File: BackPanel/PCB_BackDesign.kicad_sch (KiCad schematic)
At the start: 25 parts, among them J1 Conn_01x08_Pin, J2 Conn_01x09_Pin, J3 Conn_01x02_Pin, J4 Conn_01x02_Pin, SW1 KS11R23CQD, SW2 KS11R23CQD, SW3 KS11R23CQD

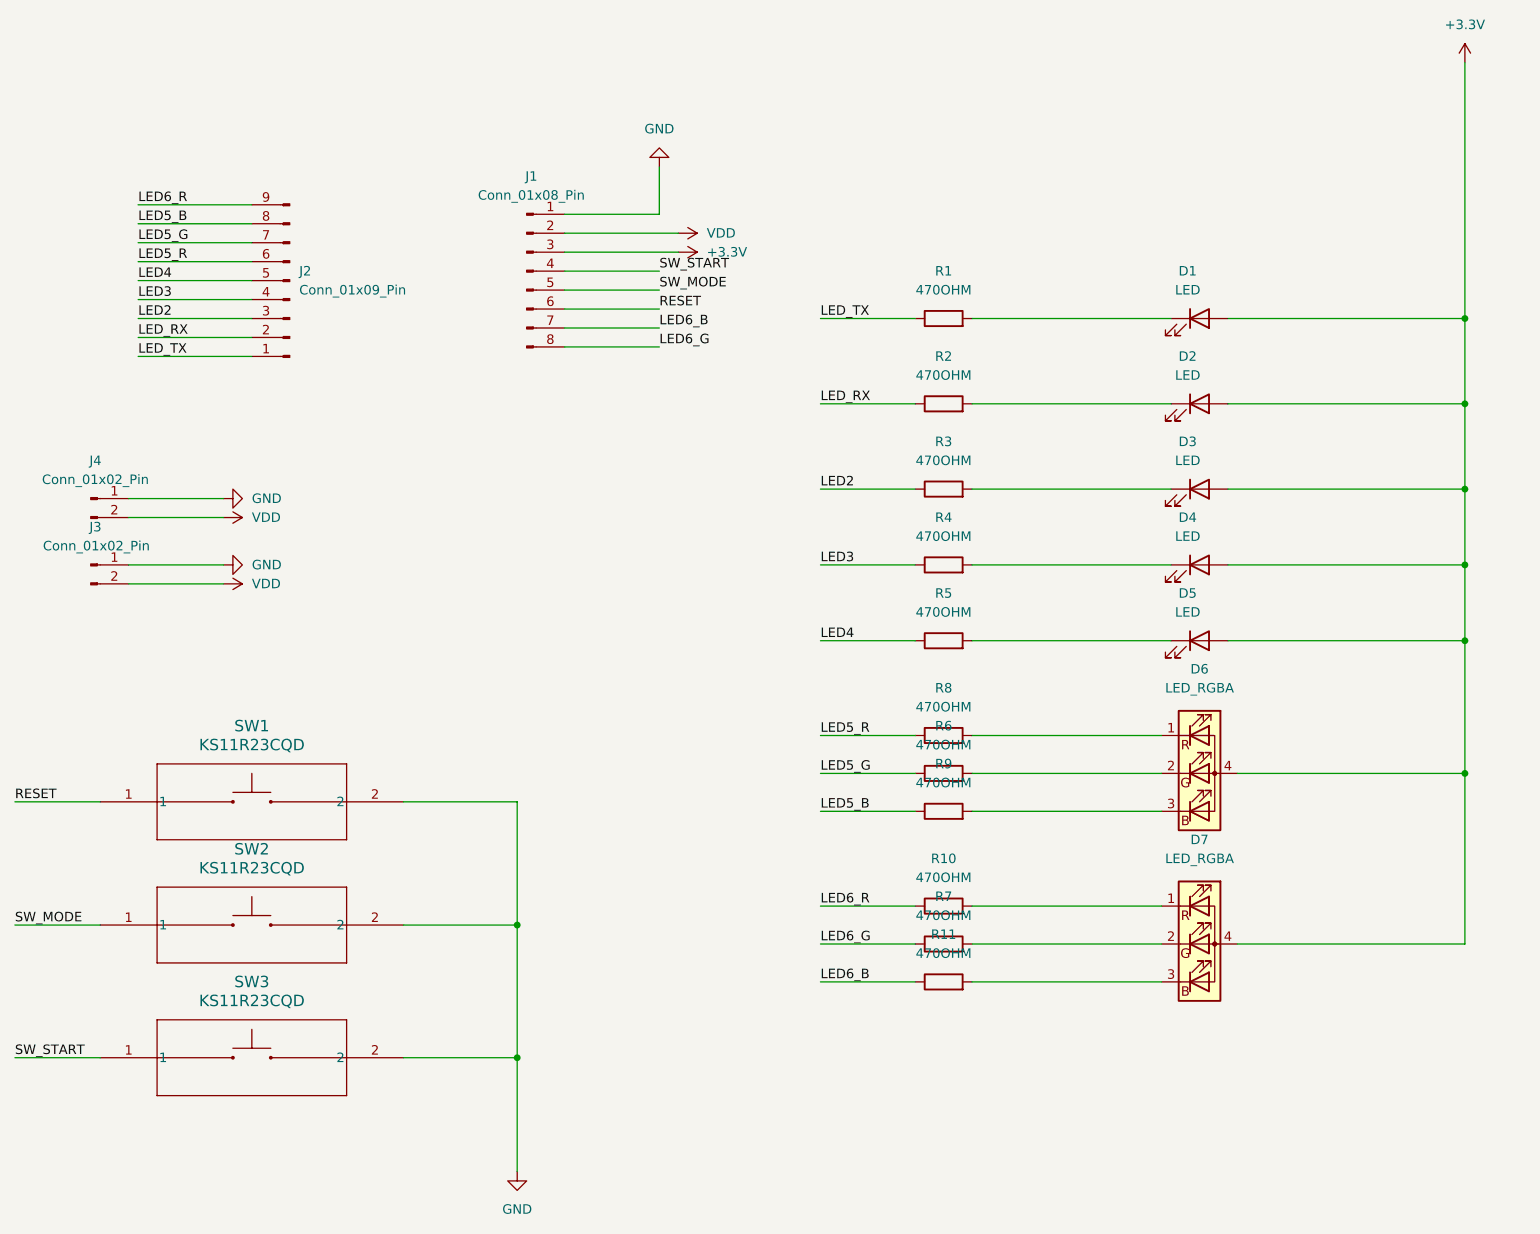
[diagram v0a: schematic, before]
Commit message: Tidied up some designators; moved two traces on the top layer to pass
DRC.
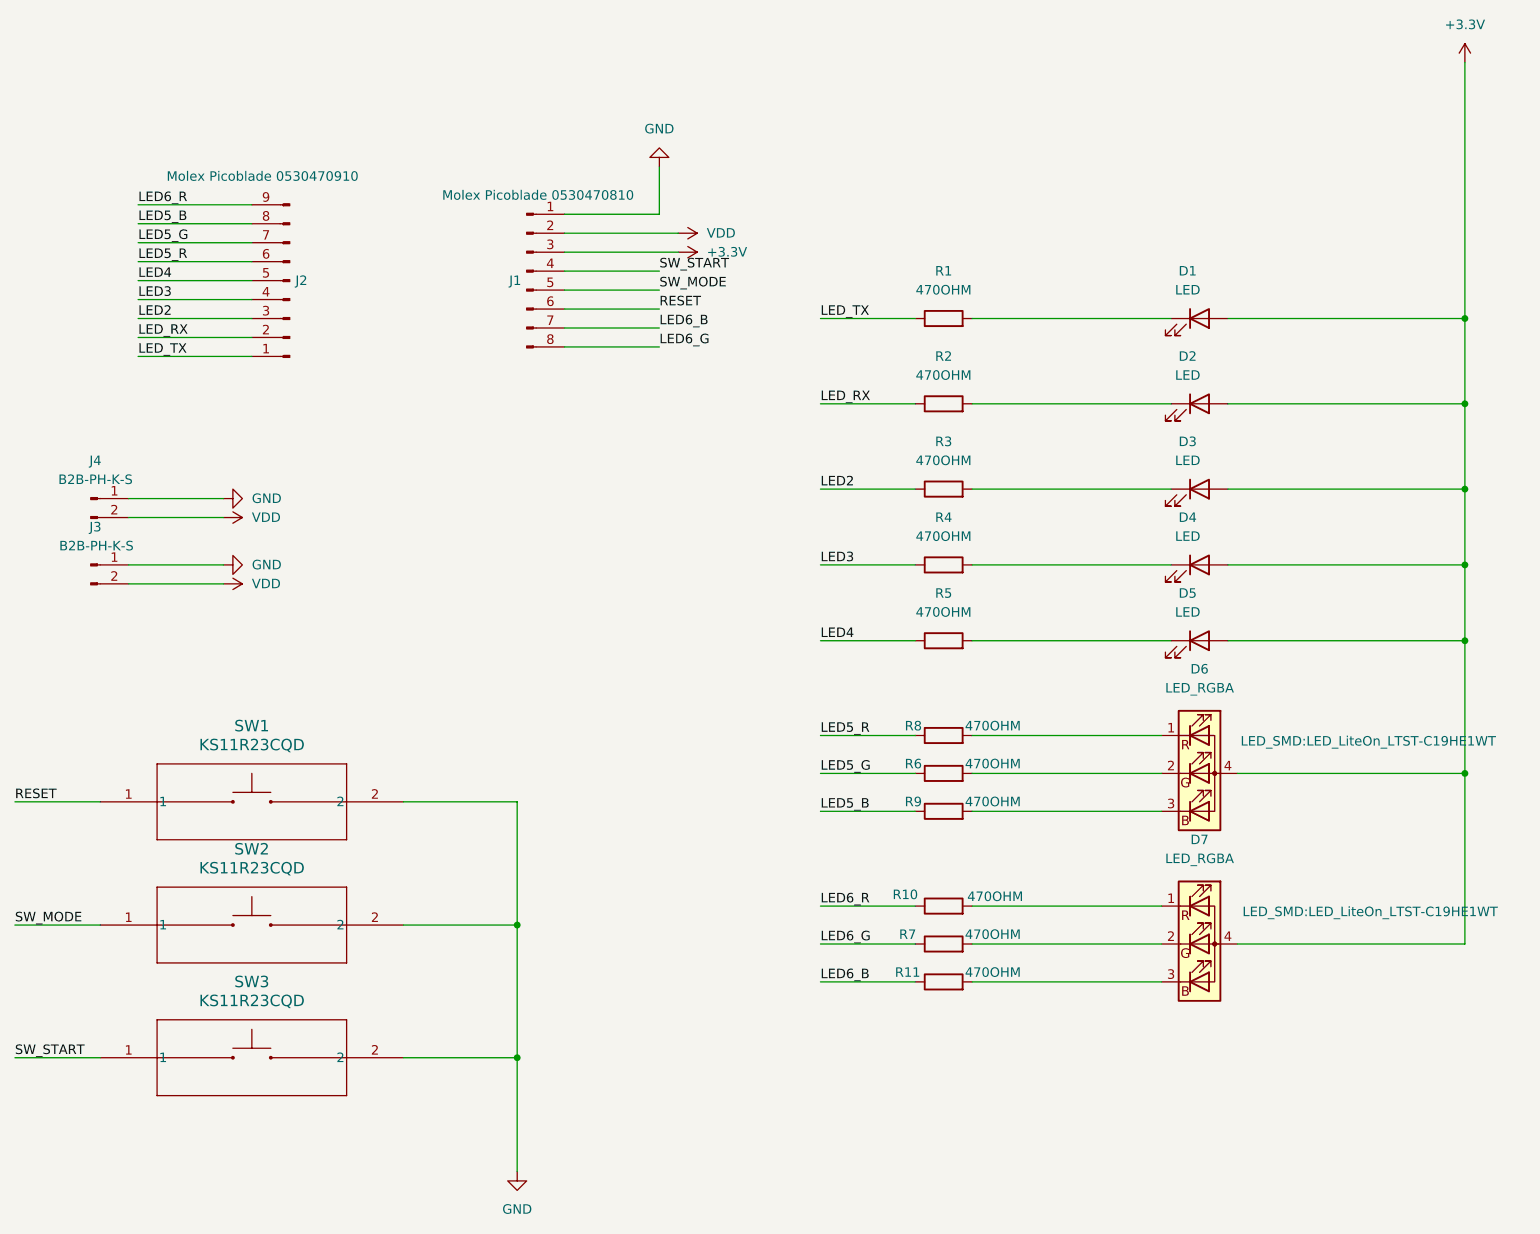
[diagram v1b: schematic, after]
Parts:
- J1: value Conn_01x08_Pin -> Molex Picoblade 0530470810
- J2: value Conn_01x09_Pin -> Molex Picoblade 0530470910
- J3, J4: value Conn_01x02_Pin -> B2B-PH-K-S
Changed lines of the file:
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@@
 		(on_board yes)
 		(dnp no)
-		(fields_autoplaced yes)
 		(property "Reference" "R10"
-			(at 184.15 132.08 90)
-			(effects
-				(font
-					(size 1.27 1.27)
-				)
+			(at 177.292 136.906 90)
+			(effects
+				(font
+					(size 1.27 1.27)
+				)
+				(justify right)
 			)
 		)
 		(property "Value" "470OHM"
-			(at 184.15 134.62 90)
-			(effects
-				(font
-					(size 1.27 1.27)
-				)
+			(at 194.818 137.16 90)
+			(effects
+				(font
+					(size 1.27 1.27)
+				)
+				(justify left)
 			)
 		)
@@
 		(on_board yes)
 		(dnp no)
-		(fields_autoplaced yes)
 		(property "Reference" "R9"
-			(at 184.15 119.38 90)
+			(at 180.086 124.46 90)
 			(effects
 				(font
@@
 		)
 		(property "Value" "470OHM"
-			(at 184.15 121.92 90)
+			(at 190.754 124.46 90)
 			(effects
 				(font
@@
 			)
 		)
-		(property "Value" "Conn_01x02_Pin"
+		(property "Value" "B2B-PH-K-S"
 			(at 70.612 90.17 0)
 			(effects
@@
 			)
 		)
-		(property "Datasheet" "~"
+		(property "Datasheet" "https://www.jst-mfg.com/product/pdf/eng/ePH.pdf"
 			(at 69.85 92.71 0)
 			(effects
@@
 		(on_board yes)
 		(dnp no)
-		(fields_autoplaced yes)
 		(property "Reference" "R11"
-			(at 184.15 142.24 90)
+			(at 179.324 147.32 90)
 			(effects
 				(font
@@
 		)
 		(property "Value" "470OHM"
-			(at 184.15 144.78 90)
+			(at 190.754 147.32 90)
 			(effects
 				(font
@@
 		(on_board yes)
 		(dnp no)
-		(fields_autoplaced yes)
 		(property "Reference" "D7"
 			(at 218.44 129.54 0)
@@
 		)
 		(property "Footprint" "LED_SMD:LED_LiteOn_LTST-C19HE1WT"
-			(at 218.44 144.78 0)
-			(effects
-				(font
-					(size 1.27 1.27)
-				)
-				(hide yes)
+			(at 241.3 139.192 0)
+			(effects
+				(font
+					(size 1.27 1.27)
+				)
 			)
 		)
@@
 		(on_board yes)
 		(dnp no)
-		(fields_autoplaced yes)
 		(property "Reference" "R7"
-			(at 184.15 137.16 90)
+			(at 179.324 142.24 90)
 			(effects
 				(font
@@
 		)
 		(property "Value" "470OHM"
-			(at 184.15 139.7 90)
+			(at 190.754 142.24 90)
 			(effects
 				(font
@@
 		(on_board yes)
 		(dnp no)
-		(fields_autoplaced yes)
 		(property "Reference" "R6"
-			(at 184.15 114.3 90)
+			(at 180.086 119.38 90)
 			(effects
 				(font
@@
 		)
 		(property "Value" "470OHM"
-			(at 184.15 116.84 90)
+			(at 190.754 119.38 90)
 			(effects
 				(font
@@
 		(on_board yes)
 		(dnp no)
-		(fields_autoplaced yes)
 		(property "Reference" "J1"
-			(at 128.905 40.64 0)
-			(effects
-				(font
-					(size 1.27 1.27)
-				)
-			)
-		)
-		(property "Value" "Conn_01x08_Pin"
-			(at 128.905 43.18 0)
+			(at 126.746 54.61 0)
+			(effects
+				(font
+					(size 1.27 1.27)
+				)
+			)
+		)
+		(property "Value" "Molex Picoblade 0530470810"
+			(at 129.794 43.18 0)
 			(effects
 				(font
@@
 			)
 		)
-		(property "Datasheet" "~"
+		(property "Datasheet" "https://www.molex.com/content/dam/molex/molex-dot-com/products/automated/en-us/salesdrawingpdf/530/53047/530470810_sd.pdf?inline"
 			(at 128.27 53.34 0)
 			(effects
@@
 		(on_board yes)
 		(dnp no)
-		(fields_autoplaced yes)
 		(property "Reference" "D6"
 			(at 218.44 106.68 0)
@@
 		)
 		(property "Footprint" "LED_SMD:LED_LiteOn_LTST-C19HE1WT"
-			(at 218.44 121.92 0)
-			(effects
-				(font
-					(size 1.27 1.27)
-				)
-				(hide yes)
+			(at 241.046 116.332 0)
+			(effects
+				(font
+					(size 1.27 1.27)
+				)
 			)
 		)
@@
 		(on_board yes)
 		(dnp no)
-		(fields_autoplaced yes)
 		(property "Reference" "J2"
-			(at 97.79 53.3399 0)
+			(at 97.282 54.61 0)
 			(effects
 				(font
@@
 			)
 		)
-		(property "Value" "Conn_01x09_Pin"
-			(at 97.79 55.8799 0)
+		(property "Value" "Molex Picoblade 0530470910"
+			(at 80.01 40.64 0)
 			(effects
 				(font
@@
 			)
 		)
-		(property "Datasheet" "~"
+		(property "Datasheet" "https://www.molex.com/content/dam/molex/molex-dot-com/products/automated/en-us/salesdrawingpdf/530/53047/530470910_sd.pdf?inline"
 			(at 96.52 54.61 0)
 			(effects
@@
 			)
 		)
-		(property "Value" "Conn_01x02_Pin"
+		(property "Value" "B2B-PH-K-S"
 			(at 70.485 81.28 0)
 			(effects
@@
 			)
 		)
-		(property "Datasheet" "~"
+		(property "Datasheet" "https://www.jst-mfg.com/product/pdf/eng/ePH.pdf"
 			(at 69.85 83.82 0)
 			(effects
@@
 		(on_board yes)
 		(dnp no)
-		(fields_autoplaced yes)
 		(property "Reference" "R8"
-			(at 184.15 109.22 90)
+			(at 180.086 114.3 90)
 			(effects
 				(font
@@
 		)
 		(property "Value" "470OHM"
-			(at 184.15 111.76 90)
-			(effects
-				(font
+			(at 190.754 114.3 90)
+			(effects
+				(font

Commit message: Added colours to the schematic.
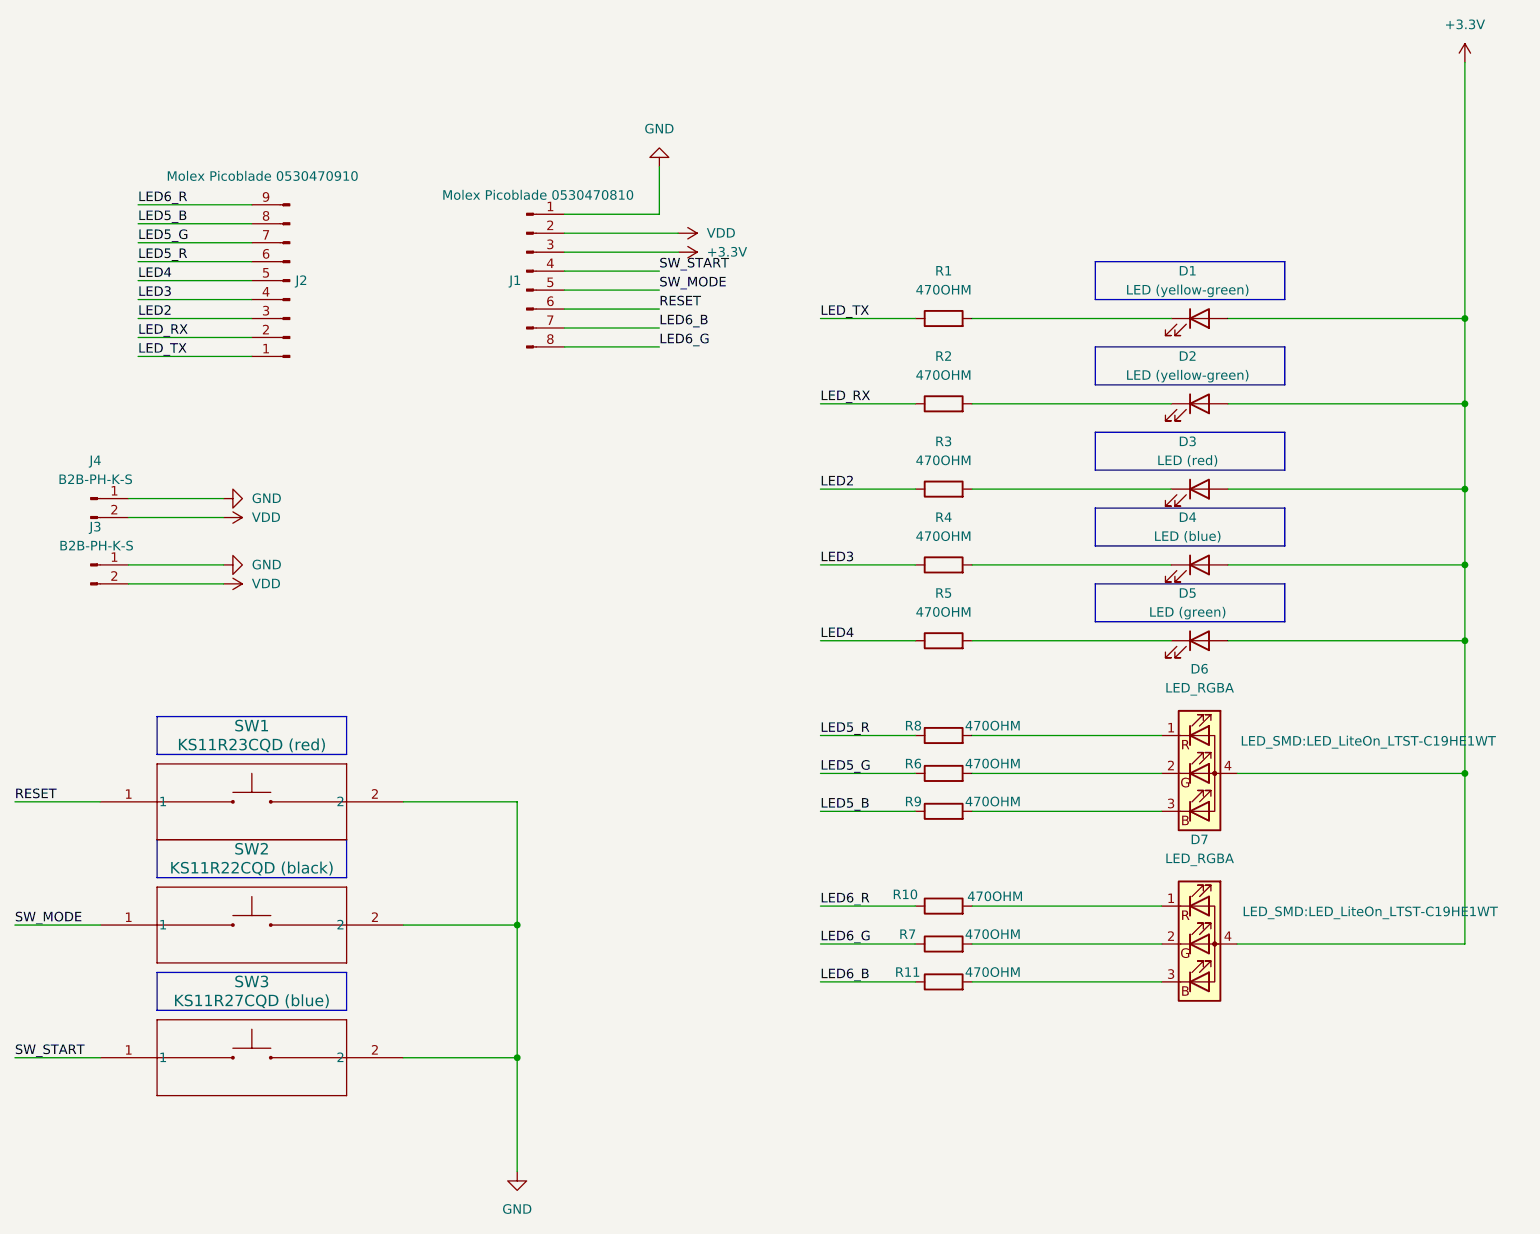
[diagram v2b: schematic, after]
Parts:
- D1, D2: value LED -> LED (yellow-green)
- D3: value LED -> LED (red)
- D4: value LED -> LED (blue)
- D5: value LED -> LED (green)
- SW1: value KS11R23CQD -> KS11R23CQD (red)
- SW2: value KS11R23CQD -> KS11R22CQD (black)
- SW3: value KS11R23CQD -> KS11R27CQD (blue)
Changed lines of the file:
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@@
+		)
+	)
+	(rectangle
+		(start 78.74 129.54)
+		(end 104.14 134.62)
+		(stroke
+			(width 0)
+			(type default)
+			(color 128 128 128 1)
+		)
+		(fill
+			(type color)
+			(color 191 191 191 1)
+		)
+	)
+	(rectangle
+		(start 204.47 63.5)
+		(end 229.87 68.58)
+		(stroke
+			(width 0)
+			(type default)
+			(color 192 255 128 1)
+		)
+		(fill
+			(type color)
+			(color 223 255 191 1)
+		)
+	)
+	(rectangle
+		(start 204.47 74.93)
+		(end 229.87 80.01)
+		(stroke
+			(width 0)
+			(type default)
+			(color 255 128 128 1)
+		)
+		(fill
+			(type color)
+			(color 255 191 191 1)
+		)
+	)
+	(rectangle
+		(start 78.74 147.32)
+		(end 104.14 152.4)
+		(stroke
+			(width 0)
+			(type default)
+			(color 128 128 255 1)
+		)
+		(fill
+			(type color)
+			(color 191 191 255 1)
+		)
+	)
+	(rectangle
+		(start 204.47 85.09)
+		(end 229.87 90.17)
+		(stroke
+			(width 0)
+			(type default)
+			(color 128 128 255 1)
+		)
+		(fill
+			(type color)
+			(color 191 191 255 1)
+		)
+	)
+	(rectangle
+		(start 204.47 95.25)
+		(end 229.87 100.33)
+		(stroke
+			(width 0)
+			(type default)
+			(color 128 255 128 1)
+		)
+		(fill
+			(type color)
+			(color 191 255 191 1)
+		)
+	)
+	(rectangle
+		(start 204.47 52.07)
+		(end 229.87 57.15)
+		(stroke
+			(width 0)
+			(type default)
+			(color 192 255 128 1)
+		)
+		(fill
+			(type color)
+			(color 223 255 191 1)
+		)
+	)
+	(rectangle
+		(start 78.74 113.03)
+		(end 104.14 118.11)
+		(stroke
+			(width 0)
+			(type default)
+			(color 255 128 128 1)
+		)
+		(fill
+			(type color)
+			(color 255 191 191 1)
 		)
 	)
@@
 			)
 		)
-		(property "Value" "LED"
+		(property "Value" "LED (green)"
 			(at 216.8525 99.06 0)
 			(effects
@@
 			)
 		)
-		(property "Value" "KS11R23CQD"
+		(property "Value" "KS11R22CQD (black)"
 			(at 91.44 133.35 0)
 			(effects
@@
 			)
 		)
-		(property "Value" "KS11R23CQD"
+		(property "Value" "KS11R27CQD (blue)"
 			(at 91.44 151.13 0)
 			(effects
@@
 			)
 		)
-		(property "Value" "LED"
+		(property "Value" "LED (yellow-green)"
 			(at 216.8525 55.88 0)
 			(effects
@@
 			)
 		)
-		(property "Value" "LED"
+		(property "Value" "LED (yellow-green)"
 			(at 216.8525 67.31 0)
 			(effects
@@
 			)
 		)
-		(property "Value" "LED"
+		(property "Value" "LED (red)"
 			(at 216.8525 78.74 0)
 			(effects
@@
 			)
 		)
-		(property "Value" "LED"
+		(property "Value" "LED (blue)"
 			(at 216.8525 88.9 0)
 			(effects
@@
 			)
 		)
-		(property "Value" "KS11R23CQD"
+		(property "Value" "KS11R23CQD (red)"
 			(at 91.44 116.84 0)
 			(effects

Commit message: Fixed the imported switch component.
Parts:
- SW1, SW2, SW3: footprint footprints:KS11_CNK -> KS11_CNK; symbol KS11R23CQD:KS11R23CQD -> KS11_CNK:KS11R23CQD
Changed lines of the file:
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@@
 	)
 	(symbol
-		(lib_id "KS11R23CQD:KS11R23CQD")
+		(lib_id "KS11_CNK:KS11R23CQD")
 		(at 71.12 140.97 0)
 		(unit 1)
@@
 			)
 		)
-		(property "Footprint" "footprints:KS11_CNK"
+		(property "Footprint" "KS11_CNK"
 			(at 71.12 140.97 0)
 			(effects
@@
 	)
 	(symbol
-		(lib_id "KS11R23CQD:KS11R23CQD")
+		(lib_id "KS11_CNK:KS11R23CQD")
 		(at 71.12 158.75 0)
 		(unit 1)
@@
 			)
 		)
-		(property "Footprint" "footprints:KS11_CNK"
+		(property "Footprint" "KS11_CNK"
 			(at 71.12 158.75 0)
 			(effects
@@
 	)
 	(symbol
-		(lib_id "KS11R23CQD:KS11R23CQD")
+		(lib_id "KS11_CNK:KS11R23CQD")
 		(at 71.12 124.46 0)
 		(unit 1)
@@
 			)
 		)
-		(property "Footprint" "footprints:KS11_CNK"
+		(property "Footprint" "KS11_CNK"
 			(at 71.12 124.46 0)
 			(effects
